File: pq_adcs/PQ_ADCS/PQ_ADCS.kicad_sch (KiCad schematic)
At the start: 51 parts, among them J1 CES-110-02-L-S, J10 Pico-Clasp_01x09, J11 Pico-Clasp_01x15, J12 CES-102-02-L-S, J2 CES-110-02-L-S, J3 CES-110-02-L-S, J4 CES-110-02-L-S, J5 Pico-Clasp_01x03, J6 Pico-Clasp_01x10, J7 Pico-Clasp_01x10, J8 Pico-Clasp_01x10, J9 Pico-Clasp_01x10, U2 LPV542, U3 LPV542, U4 IIM-42652, U5 BD2606MVV, U6 TMUX1108RSVR, U7 MMC5983MA

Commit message: change C15 package from 0603 to 0805
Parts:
- C15: footprint Capacitor_SMD:C_0603_1608Metric -> Capacitor_SMD:C_0805_2012Metric
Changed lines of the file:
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@@
       (effects (font (size 1.27 1.27)) (justify right))
     )
-    (property "Footprint" "Capacitor_SMD:C_0603_1608Metric" (at 124.1552 133.35 0)
+    (property "Footprint" "Capacitor_SMD:C_0805_2012Metric" (at 124.1552 133.35 0)
       (effects (font (size 1.27 1.27)) hide)
     )

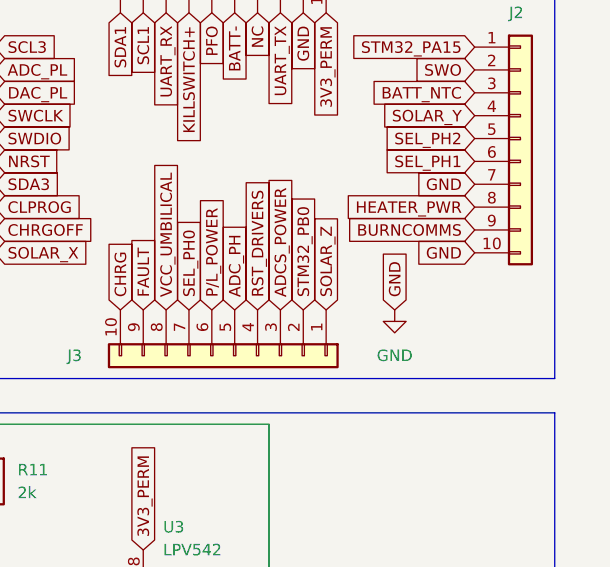
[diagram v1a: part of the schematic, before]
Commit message: swap SOLARZ with GND
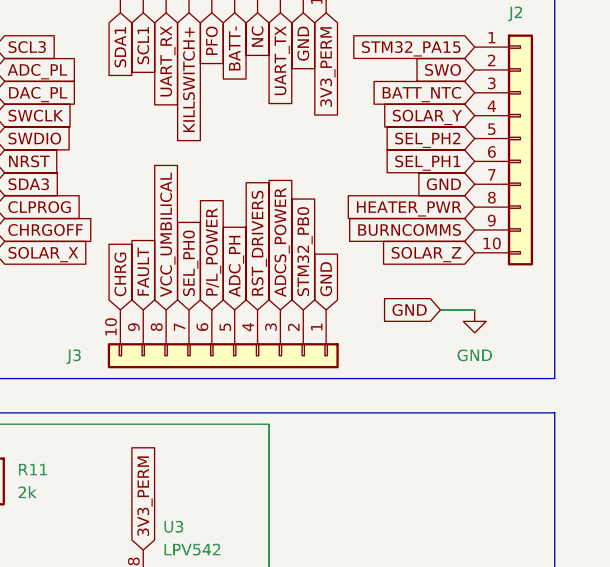
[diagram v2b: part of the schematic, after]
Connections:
- net GND: now also J3.1 (Pin_1); no longer J2.10 (Pin_10)
- net SOLAR_Z: now also J2.10 (Pin_10); no longer J3.1 (Pin_1)
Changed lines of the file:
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@@
+    (stroke (width 0) (type default))
+  )
+  (wire (pts (xy 267.97 57.15) (xy 271.78 57.15))
     (stroke (width 0) (type default))
   )
@@
     )
   )
-  (global_label "GND" (shape input) (at 271.78 50.8 180) (fields_autoplaced)
-    (effects (font (size 1.27 1.27)) (justify right))
-    (property "Intersheetrefs" "${INTERSHEET_REFS}" (at 265.4964 50.7206 0)
+  (global_label "SOLAR_Z" (shape input) (at 271.78 50.8 180) (fields_autoplaced)
+    (effects (font (size 1.27 1.27)) (justify right))
+    (property "Intersheetrefs" "${INTERSHEET_REFS}" (at 260.691 50.8 0)
       (effects (font (size 1.27 1.27)) (justify right) hide)
     )
@@
     )
   )
-  (global_label "GND" (shape input) (at 262.89 57.15 90) (fields_autoplaced)
-    (effects (font (size 1.27 1.27)) (justify left))
-    (property "Intersheetrefs" "${INTERSHEET_REFS}" (at 262.8106 50.8664 90)
-      (effects (font (size 1.27 1.27)) (justify left) hide)
+  (global_label "GND" (shape input) (at 267.97 57.15 180) (fields_autoplaced)
+    (effects (font (size 1.27 1.27)) (justify right))
+    (property "Intersheetrefs" "${INTERSHEET_REFS}" (at 261.1143 57.15 0)
+      (effects (font (size 1.27 1.27)) (justify right) hide)
     )
   )
@@
     )
   )
-  (global_label "SOLAR_Z" (shape input) (at 255.27 57.15 90) (fields_autoplaced)
-    (effects (font (size 1.27 1.27)) (justify left))
-    (property "Intersheetrefs" "${INTERSHEET_REFS}" (at 255.1906 46.6331 90)
+  (global_label "GND" (shape input) (at 255.27 57.15 90) (fields_autoplaced)
+    (effects (font (size 1.27 1.27)) (justify left))
+    (property "Intersheetrefs" "${INTERSHEET_REFS}" (at 255.27 50.2943 90)
       (effects (font (size 1.27 1.27)) (justify left) hide)
     )
@@
     )
   )
-  (symbol (lib_name "GND_36") (lib_id "power:GND") (at 262.89 57.15 0) (unit 1)
+  (symbol (lib_name "GND_36") (lib_id "power:GND") (at 271.78 57.15 0) (unit 1)
     (in_bom yes) (on_board yes) (dnp no) (fields_autoplaced)
-    (property "Reference" "#PWR0112" (at 262.89 63.5 0)
-      (effects (font (size 1.27 1.27)) hide)
-    )
-    (property "Value" "GND" (at 262.89 62.23 0)
+    (property "Reference" "#PWR0112" (at 271.78 63.5 0)
+      (effects (font (size 1.27 1.27)) hide)
+    )
+    (property "Value" "GND" (at 271.78 62.23 0)
       (effects (font (size 1.27 1.27)))
     )
-    (property "Footprint" "" (at 262.89 57.15 0)
-      (effects (font (size 1.27 1.27)) hide)
-    )
-    (property "Datasheet" "" (at 262.89 57.15 0)
-      (effects (font (size 1.27 1.27)) hide)
-    )
+    (property "Footprint" "" (at 271.78 57.15 0)
+      (effects (font (size 1.27 1.27)) hide)
+    )
+    (property "Datasheet" "" (at 271.78 57.15 0)
+      (effects (font (size 1.27 1.27)) hide)
+    )

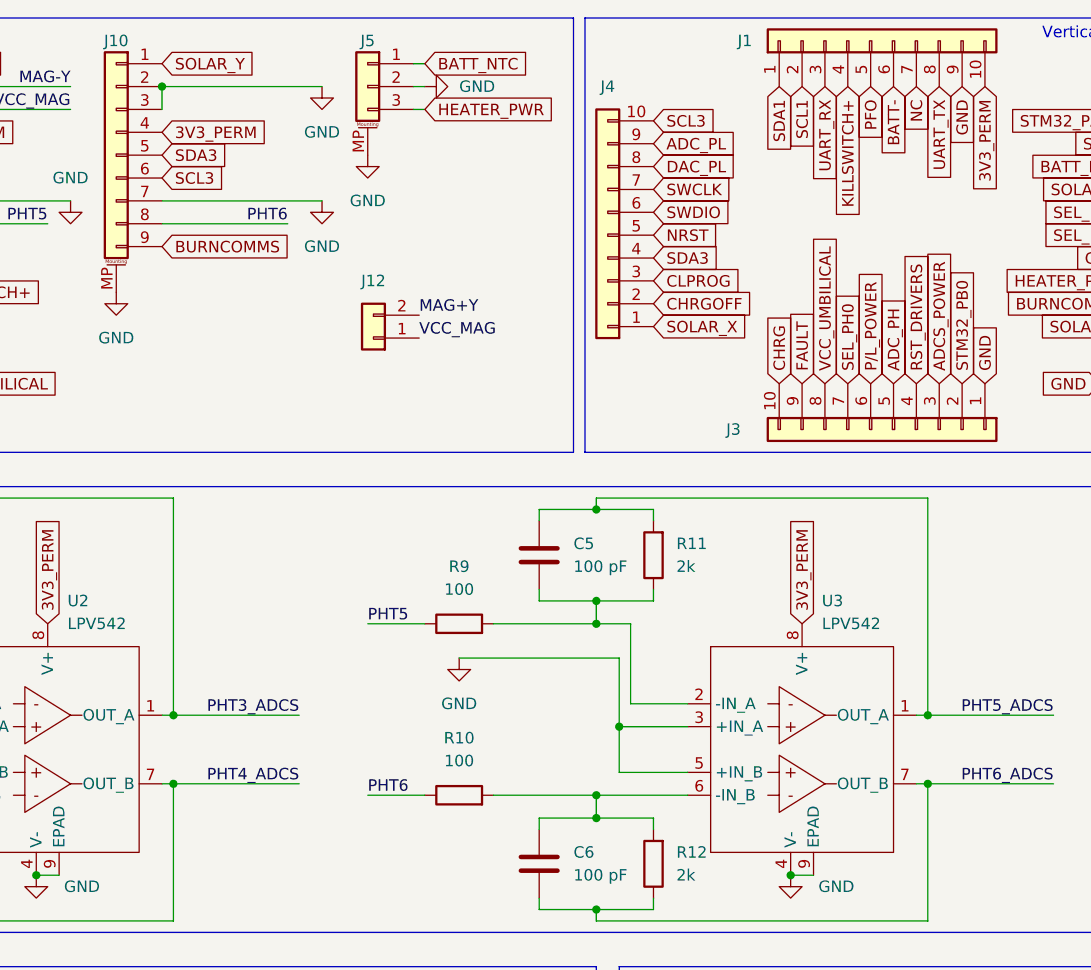
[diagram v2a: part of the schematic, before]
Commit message: change pin RST_DRIVERS to STM32_PA9, swap SCL3 with NC and redirect all IC to new SCL3 location. Change NC pin to PH_PL, substitute PHT6 to PH_PL and small fixes
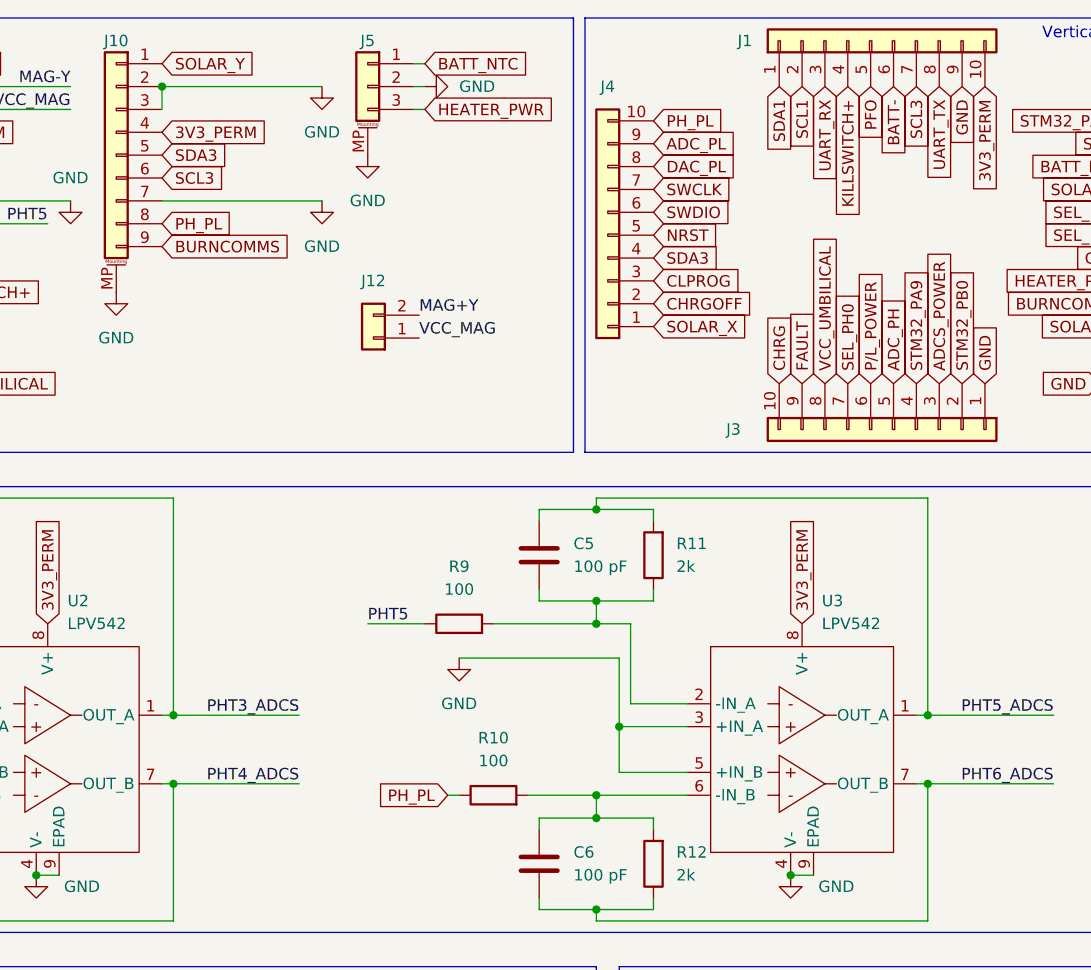
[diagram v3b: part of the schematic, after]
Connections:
- net NC is gone; now on net SCL3: J1.7 (Pin_7)
- net SCL3: no longer J4.10 (Pin_10)
- net PHT6 renamed PH_PL
- net PH_PL: now also J4.10 (Pin_10)
- net RST_DRIVERS renamed STM32_PA9
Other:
- moved on the sheet: R10
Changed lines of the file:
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@@
     (stroke (width 0) (type default))
   )
-  (wire (pts (xy 177.8 39.37) (xy 163.83 39.37))
-    (stroke (width 0) (type default))
-  )
-  (wire (pts (xy 200.66 102.87) (xy 212.09 102.87))
+  (wire (pts (xy 204.47 102.87) (xy 212.09 102.87))
     (stroke (width 0) (type default))
   )
@@
     (stroke (width 0) (type default))
   )
-  (wire (pts (xy 186.69 102.87) (xy 193.04 102.87))
-    (stroke (width 0) (type default))
-  )
   (wire (pts (xy 44.45 71.12) (xy 44.45 69.85))
     (stroke (width 0) (type default))
@@
     (stroke (width 0) (type default))
   )
+  (wire (pts (xy 195.58 102.87) (xy 196.85 102.87))
+    (stroke (width 0) (type default))
+  )
   (wire (pts (xy 177.8 158.75) (xy 180.34 158.75))
     (stroke (width 0) (type default))
@@
     (effects (font (size 1.27 1.27)) (justify right bottom))
   )
-  (label "PHT6" (at 177.8 39.37 180) (fields_autoplaced)
-    (effects (font (size 1.27 1.27)) (justify right bottom))
-  )
   (label "PHT1" (at 38.1 39.37 180) (fields_autoplaced)
     (effects (font (size 1.27 1.27)) (justify right bottom))
@@
     (effects (font (size 1.27 1.27)) (justify left bottom))
   )
-  (label "PHT6" (at 186.69 102.87 0) (fields_autoplaced)
-    (effects (font (size 1.27 1.27)) (justify left bottom))
-  )
   (label "VCC_MAG" (at 192.405 52.07 0) (fields_autoplaced)
     (effects (font (size 1.27 1.27)) (justify left bottom))
@@
     )
   )
-  (global_label "RST_DRIVERS" (shape input) (at 247.65 57.15 90) (fields_autoplaced)
-    (effects (font (size 1.27 1.27)) (justify left))
-    (property "Intersheetrefs" "${INTERSHEET_REFS}" (at 247.5706 42.4602 90)
+  (global_label "STM32_PA9" (shape input) (at 247.65 57.15 90) (fields_autoplaced)
+    (effects (font (size 1.27 1.27)) (justify left))
+    (property "Intersheetrefs" "${INTERSHEET_REFS}" (at 247.65 43.5816 90)
       (effects (font (size 1.27 1.27)) (justify left) hide)
     )
@@
     )
   )
+  (global_label "PH_PL" (shape input) (at 195.58 102.87 180) (fields_autoplaced)
+    (effects (font (size 1.27 1.27)) (justify right))
+    (property "Intersheetrefs" "${INTERSHEET_REFS}" (at 186.7286 102.87 0)
+      (effects (font (size 1.27 1.27)) (justify right) hide)
+    )
+  )
   (global_label "SEL_PH2" (shape input) (at 26.67 182.245 180) (fields_autoplaced)
     (effects (font (size 1.27 1.27)) (justify right))
@@
     )
   )
-  (global_label "NC" (shape input) (at 247.65 24.13 270) (fields_autoplaced)
-    (effects (font (size 1.27 1.27)) (justify right))
-    (property "Intersheetrefs" "${INTERSHEET_REFS}" (at 247.65 29.7157 90)
+  (global_label "SCL3" (shape input) (at 247.65 24.13 270) (fields_autoplaced)
+    (effects (font (size 1.27 1.27)) (justify right))
+    (property "Intersheetrefs" "${INTERSHEET_REFS}" (at 247.65 31.8323 90)
       (effects (font (size 1.27 1.27)) (justify right) hide)
     )
@@
     )
   )
-  (global_label "SCL3" (shape input) (at 218.44 27.94 0) (fields_autoplaced)
-    (effects (font (size 1.27 1.27)) (justify left))
-    (property "Intersheetrefs" "${INTERSHEET_REFS}" (at 225.5702 27.8606 0)
+  (global_label "PH_PL" (shape input) (at 218.44 27.94 0) (fields_autoplaced)
+    (effects (font (size 1.27 1.27)) (justify left))
+    (property "Intersheetrefs" "${INTERSHEET_REFS}" (at 227.2914 27.94 0)
       (effects (font (size 1.27 1.27)) (justify left) hide)
     )
@@
     (effects (font (size 1.27 1.27)) (justify left))
     (property "Intersheetrefs" "${INTERSHEET_REFS}" (at 207.3669 26.7494 0)
+      (effects (font (size 1.27 1.27)) (justify left) hide)
+    )
+  )
+  (global_label "PH_PL" (shape input) (at 163.83 39.37 0) (fields_autoplaced)
+    (effects (font (size 1.27 1.27)) (justify left))
+    (property "Intersheetrefs" "${INTERSHEET_REFS}" (at 172.6814 39.37 0)
       (effects (font (size 1.27 1.27)) (justify left) hide)
     )
@@
     )
   )
-  (symbol (lib_id "Device:R") (at 196.85 102.87 90) (unit 1)
+  (symbol (lib_id "Device:R") (at 200.66 102.87 90) (unit 1)
     (in_bom yes) (on_board yes) (dnp no) (fields_autoplaced)
-    (property "Reference" "R10" (at 196.85 96.52 90)
+    (property "Reference" "R10" (at 200.66 96.52 90)
       (effects (font (size 1.27 1.27)))
     )
-    (property "Value" "100" (at 196.85 99.06 90)
+    (property "Value" "100" (at 200.66 99.06 90)
       (effects (font (size 1.27 1.27)))
     )
-    (property "Footprint" "Resistor_SMD:R_0603_1608Metric" (at 196.85 104.648 90)
-      (effects (font (size 1.27 1.27)) hide)
-    )
-    (property "Datasheet" "~" (at 196.85 102.87 0)
-      (effects (font (size 1.27 1.27)) hide)
-    )
-    (property "Manufacturer 1" "YAGEO" (at 196.85 102.87 0)
-      (effects (font (size 1.27 1.27)) hide)
-    )
-    (property "Manufacturer Part Number 1" "AC0603FR-13100RL" (at 196.85 102.87 0)
-      (effects (font (size 1.27 1.27)) hide)
-    )
-    (property "Supplier 1" "Mouser" (at 196.85 102.87 0)
-      (effects (font (size 1.27 1.27)) hide)
-    )
-    (property "Supplier Part Number 1" "603-AC0603FR-13100RL" (at 196.85 102.87 0)
-      (effects (font (size 1.27 1.27)) hide)
-    )
+    (property "Footprint" "Resistor_SMD:R_0603_1608Metric" (at 200.66 104.648 90)
+      (effects (font (size 1.27 1.27)) hide)
+    )
+    (property "Datasheet" "~" (at 200.66 102.87 0)
+      (effects (font (size 1.27 1.27)) hide)
+    )
+    (property "Manufacturer 1" "YAGEO" (at 200.66 102.87 0)
+      (effects (font (size 1.27 1.27)) hide)
+    )
+    (property "Manufacturer Part Number 1" "AC0603FR-13100RL" (at 200.66 102.87 0)
+      (effects (font (size 1.27 1.27)) hide)
+    )
+    (property "Supplier 1" "Mouser" (at 200.66 102.87 0)
+      (effects (font (size 1.27 1.27)) hide)
+    )
+    (property "Supplier Part Number 1" "603-AC0603FR-13100RL" (at 200.66 102.87 0)
+      (effects (font (size 1.27 1.27)) hide)
+    )
